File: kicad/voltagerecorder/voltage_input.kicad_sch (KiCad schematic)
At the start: 11 parts

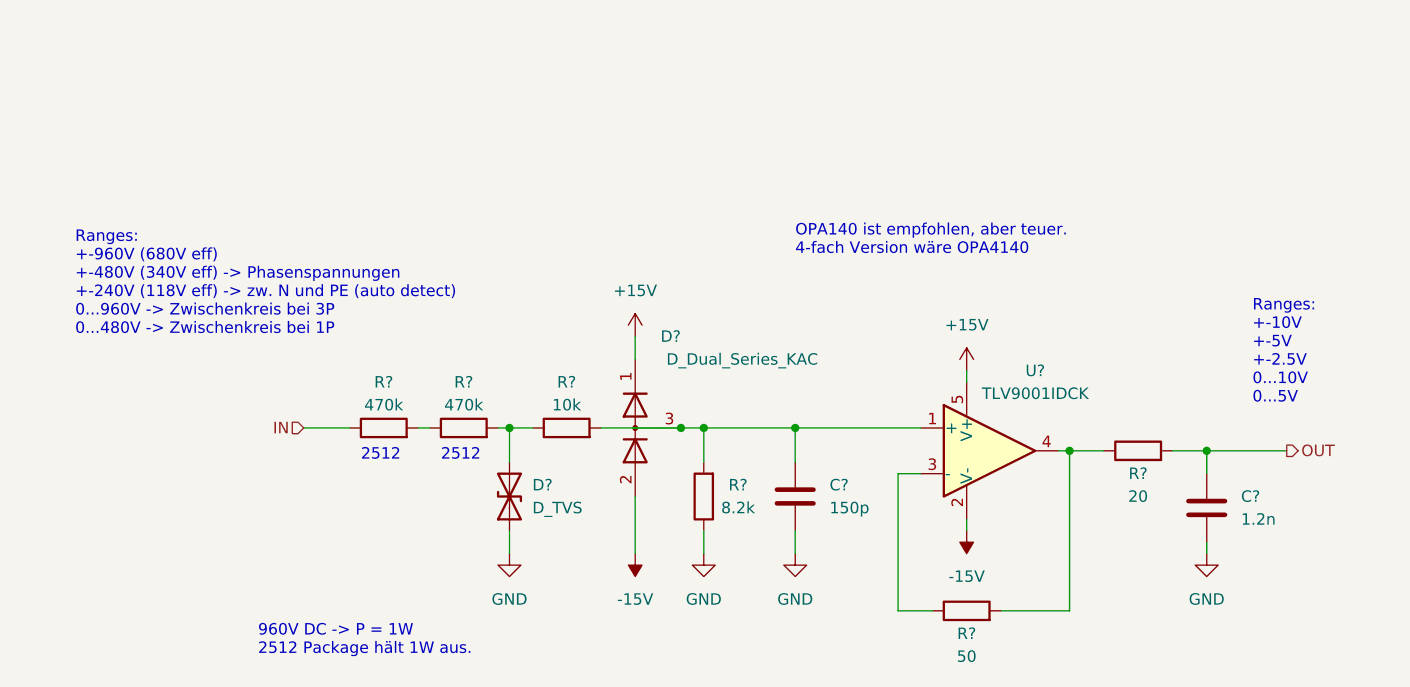
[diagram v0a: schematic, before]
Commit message: Schematic as pdf added.
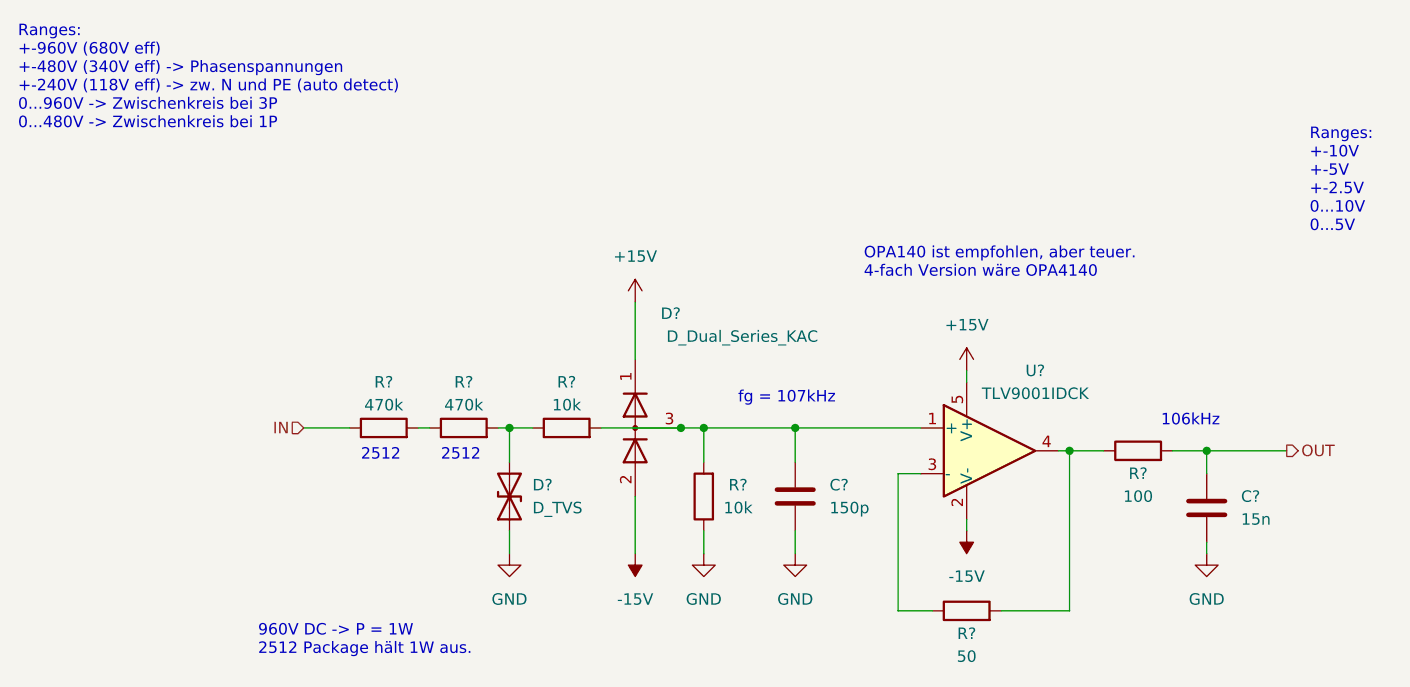
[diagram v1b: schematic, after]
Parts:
- C?: value 1.2n -> 15n
- R?: value 20 -> 100
- R?: value 8.2k -> 10k
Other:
- note added: "106kHz"
- note added: "fg = 107kHz"
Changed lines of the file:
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@@
     (stroke (width 0) (type default) (color 0 0 0 0))
   )
-  (wire (pts (xy 132.08 82.55) (xy 132.08 85.09))
+  (wire (pts (xy 132.08 78.74) (xy 132.08 85.09))
     (stroke (width 0) (type default) (color 0 0 0 0))
   )
@@
   )
   (text "Ranges:\n+-960V (680V eff)\n+-480V (340V eff) -> Phasenspannungen\n+-240V (118V eff) -> zw. N und PE (auto detect)\n0...960V -> Zwischenkreis bei 3P\n0...480V -> Zwischenkreis bei 1P\n"
-    (at 69.85 82.55 0)
+    (at 63.5 59.69 0)
     (effects (font (size 1.27 1.27)) (justify left bottom))
   )
@@
     (effects (font (size 1.27 1.27)) (justify left bottom))
   )
+  (text "106kHz" (at 190.5 92.71 0)
+    (effects (font (size 1.27 1.27)) (justify left bottom))
+  )
   (text "OPA140 ist empfohlen, aber teuer.\n4-fach Version wäre OPA4140"
-    (at 149.86 73.66 0)
-    (effects (font (size 1.27 1.27)) (justify left bottom))
-  )
-  (text "Ranges:\n+-10V\n+-5V\n+-2.5V\n0...10V\n0...5V" (at 200.66 90.17 0)
+    (at 157.48 76.2 0)
+    (effects (font (size 1.27 1.27)) (justify left bottom))
+  )
+  (text "Ranges:\n+-10V\n+-5V\n+-2.5V\n0...10V\n0...5V" (at 207.01 71.12 0)
     (effects (font (size 1.27 1.27)) (justify left bottom))
   )
   (text "2512" (at 110.49 96.52 0)
+    (effects (font (size 1.27 1.27)) (justify left bottom))
+  )
+  (text "fg = 107kHz" (at 143.51 90.17 0)
     (effects (font (size 1.27 1.27)) (justify left bottom))
   )
@@
     (pin "1")
   )
-  (symbol (lib_id "power:+15V") (at 132.08 82.55 0) (unit 1)
-    (in_bom yes) (on_board yes) (fields_autoplaced)
-    (property "Reference" "#PWR?" (id 0) (at 132.08 86.36 0)
-      (effects (font (size 1.27 1.27)) hide)
-    )
-    (property "Value" "+15V" (id 1) (at 132.08 77.47 0))
-    (property "Footprint" "" (id 2) (at 132.08 82.55 0)
-      (effects (font (size 1.27 1.27)) hide)
-    )
-    (property "Datasheet" "" (id 3) (at 132.08 82.55 0)
+  (symbol (lib_id "power:+15V") (at 132.08 78.74 0) (unit 1)
+    (in_bom yes) (on_board yes)
+    (property "Reference" "#PWR?" (id 0) (at 132.08 82.55 0)
+      (effects (font (size 1.27 1.27)) hide)
+    )
+    (property "Value" "+15V" (id 1) (at 132.08 73.66 0))
+    (property "Footprint" "" (id 2) (at 132.08 78.74 0)
+      (effects (font (size 1.27 1.27)) hide)
+    )
+    (property "Datasheet" "" (id 3) (at 132.08 78.74 0)
       (effects (font (size 1.27 1.27)) hide)
     )
@@
     (in_bom yes) (on_board yes)
     (property "Reference" "R?" (id 0) (at 187.96 97.79 90))
-    (property "Value" "20" (id 1) (at 187.96 100.33 90))
+    (property "Value" "100" (id 1) (at 187.96 100.33 90))
     (property "Footprint" "" (id 2) (at 187.96 97.028 90)
       (effects (font (size 1.27 1.27)) hide)
@@
       (effects (font (size 1.27 1.27)) (justify left))
     )
-    (property "Value" "1.2n" (id 1) (at 199.39 102.8699 0)
+    (property "Value" "15n" (id 1) (at 199.39 102.8699 0)
       (effects (font (size 1.27 1.27)) (justify left))
     )
@@
   (symbol (lib_id "Device:D_Dual_Series_KAC") (at 132.08 92.71 90) (unit 1)
     (in_bom yes) (on_board yes)
-    (property "Reference" "D?" (id 0) (at 137.16 82.55 90)
-      (effects (font (size 1.27 1.27)) (justify left))
-    )
-    (property "Value" "D_Dual_Series_KAC" (id 1) (at 152.4 85.09 90)
+    (property "Reference" "D?" (id 0) (at 137.16 80.01 90)
+      (effects (font (size 1.27 1.27)) (justify left))
+    )
+    (property "Value" "D_Dual_Series_KAC" (id 1) (at 152.4 82.55 90)
       (effects (font (size 1.27 1.27)) (justify left))
     )
@@
     (in_bom yes) (on_board yes)
     (property "Reference" "R?" (id 0) (at 143.51 99.06 0))
-    (property "Value" "8.2k" (id 1) (at 143.51 101.6 0))
+    (property "Value" "10k" (id 1) (at 143.51 101.6 0))
     (property "Footprint" "" (id 2) (at 141.478 100.33 90)
       (effects (font (size 1.27 1.27)) hide)

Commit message: BOM hinzugefügt, Schaltplan editiert.
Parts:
- removed R?: 10k, symbol Device:R
- added R?: 330k, symbol Device:R
- R? (x2): value 470k -> 330k
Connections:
- net at C?.1, D?.3 (common), R?.2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: now also D?.2 (A2), R?.2
- net at R?.2: now also R?.1; no longer D?.2 (A2)
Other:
- note added: "1000V DC -> P = 1W"
- note added: "MELF"
- note removed: "2512"
- note removed: "960V DC -> P = 1W 2512 Package hält 1W aus."
- moved on the sheet: D?, R?
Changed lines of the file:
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@@
 (kicad_sch (version 20211123) (generator eeschema)
   (paper "A4")
-  (junction (at 118.11 92.71) (diameter 0) (color 0 0 0 0)
+  (junction (at 120.65 92.71) (diameter 0) (color 0 0 0 0)
   )
   (junction (at 149.86 92.71) (diameter 0) (color 0 0 0 0)
@@
   (junction (at 195.58 95.25) (diameter 0) (color 0 0 0 0)
   )
+  (wire (pts (xy 120.65 92.71) (xy 137.16 92.71))
+    (stroke (width 0) (type default) (color 0 0 0 0))
+  )
   (wire (pts (xy 180.34 95.25) (xy 184.15 95.25))
     (stroke (width 0) (type default) (color 0 0 0 0))
@@
     (stroke (width 0) (type default) (color 0 0 0 0))
   )
-  (wire (pts (xy 95.25 92.71) (xy 100.33 92.71))
+  (wire (pts (xy 120.65 92.71) (xy 120.65 96.52))
+    (stroke (width 0) (type default) (color 0 0 0 0))
+  )
+  (wire (pts (xy 83.82 92.71) (xy 88.9 92.71))
     (stroke (width 0) (type default) (color 0 0 0 0))
   )
@@
     (stroke (width 0) (type default) (color 0 0 0 0))
   )
-  (wire (pts (xy 118.11 104.14) (xy 118.11 106.68))
+  (wire (pts (xy 120.65 104.14) (xy 120.65 106.68))
     (stroke (width 0) (type default) (color 0 0 0 0))
   )
@@
     (stroke (width 0) (type default) (color 0 0 0 0))
   )
+  (wire (pts (xy 105.41 92.71) (xy 106.68 92.71))
+    (stroke (width 0) (type default) (color 0 0 0 0))
+  )
   (wire (pts (xy 195.58 95.25) (xy 195.58 97.79))
     (stroke (width 0) (type default) (color 0 0 0 0))
   )
-  (wire (pts (xy 107.95 92.71) (xy 109.22 92.71))
+  (wire (pts (xy 96.52 92.71) (xy 97.79 92.71))
     (stroke (width 0) (type default) (color 0 0 0 0))
   )
@@
     (stroke (width 0) (type default) (color 0 0 0 0))
   )
-  (wire (pts (xy 116.84 92.71) (xy 118.11 92.71))
-    (stroke (width 0) (type default) (color 0 0 0 0))
-  )
   (wire (pts (xy 161.29 113.03) (xy 165.1 113.03))
     (stroke (width 0) (type default) (color 0 0 0 0))
   )
-  (wire (pts (xy 118.11 92.71) (xy 118.11 96.52))
-    (stroke (width 0) (type default) (color 0 0 0 0))
-  )
-  (wire (pts (xy 128.27 92.71) (xy 137.16 92.71))
-    (stroke (width 0) (type default) (color 0 0 0 0))
-  )
   (wire (pts (xy 180.34 113.03) (xy 180.34 95.25))
     (stroke (width 0) (type default) (color 0 0 0 0))
   )
+  (wire (pts (xy 114.3 92.71) (xy 120.65 92.71))
+    (stroke (width 0) (type default) (color 0 0 0 0))
+  )
   (wire (pts (xy 172.72 113.03) (xy 180.34 113.03))
     (stroke (width 0) (type default) (color 0 0 0 0))
@@
     (stroke (width 0) (type default) (color 0 0 0 0))
   )
-  (wire (pts (xy 118.11 92.71) (xy 120.65 92.71))
-    (stroke (width 0) (type default) (color 0 0 0 0))
-  )
   (wire (pts (xy 149.86 92.71) (xy 163.83 92.71))
     (stroke (width 0) (type default) (color 0 0 0 0))
   )
-  (text "2512" (at 101.6 96.52 0)
+  (text "MELF" (at 90.17 96.52 0)
     (effects (font (size 1.27 1.27)) (justify left bottom))
   )
@@
     (effects (font (size 1.27 1.27)) (justify left bottom))
   )
-  (text "960V DC -> P = 1W\n2512 Package hält 1W aus." (at 90.17 118.11 0)
+  (text "MELF" (at 140.97 105.41 0)
+    (effects (font (size 1.27 1.27)) (justify left bottom))
+  )
+  (text "1000V DC -> P = 1W" (at 88.9 102.87 0)
     (effects (font (size 1.27 1.27)) (justify left bottom))
   )
   (text "106kHz" (at 190.5 92.71 0)
+    (effects (font (size 1.27 1.27)) (justify left bottom))
+  )
+  (text "MELF" (at 107.95 96.52 0)
     (effects (font (size 1.27 1.27)) (justify left bottom))
   )
@@
     (effects (font (size 1.27 1.27)) (justify left bottom))
   )
-  (text "2512" (at 110.49 96.52 0)
+  (text "MELF" (at 99.06 96.52 0)
     (effects (font (size 1.27 1.27)) (justify left bottom))
   )
@@
     (effects (font (size 1.27 1.27)) (justify left bottom))
   )
-  (hierarchical_label "IN" (shape input) (at 95.25 92.71 180)
+  (hierarchical_label "IN" (shape input) (at 83.82 92.71 180)
     (effects (font (size 1.27 1.27)) (justify right))
   )
@@
     (pin "2")
   )
-  (symbol (lib_id "Device:D_TVS") (at 118.11 100.33 90) (unit 1)
-    (in_bom yes) (on_board yes) (fields_autoplaced)
-    (property "Reference" "D?" (id 0) (at 120.65 99.0599 90)
+  (symbol (lib_id "Device:D_TVS") (at 120.65 100.33 90) (unit 1)
+    (in_bom yes) (on_board yes) (fields_autoplaced)
+    (property "Reference" "D?" (id 0) (at 123.19 99.0599 90)
       (effects (font (size 1.27 1.27)) (justify right))
     )
-    (property "Value" "D_TVS" (id 1) (at 120.65 101.5999 90)
+    (property "Value" "D_TVS" (id 1) (at 123.19 101.5999 90)
       (effects (font (size 1.27 1.27)) (justify right))
     )
-    (property "Footprint" "" (id 2) (at 118.11 100.33 0)
-      (effects (font (size 1.27 1.27)) hide)
-    )
-    (property "Datasheet" "~" (id 3) (at 118.11 100.33 0)
+    (property "Footprint" "" (id 2) (at 120.65 100.33 0)
+      (effects (font (size 1.27 1.27)) hide)
+    )
+    (property "Datasheet" "~" (id 3) (at 120.65 100.33 0)
       (effects (font (size 1.27 1.27)) hide)
     )
@@
     (pin "1")
   )
-  (symbol (lib_id "power:GND") (at 118.11 106.68 0) (unit 1)
-    (in_bom yes) (on_board yes) (fields_autoplaced)
-    (property "Reference" "#PWR?" (id 0) (at 118.11 113.03 0)
-      (effects (font (size 1.27 1.27)) hide)
-    )
-    (property "Value" "GND" (id 1) (at 118.11 111.76 0))
-    (property "Footprint" "" (id 2) (at 118.11 106.68 0)
-      (effects (font (size 1.27 1.27)) hide)
-    )
-    (property "Datasheet" "" (id 3) (at 118.11 106.68 0)
+  (symbol (lib_id "power:GND") (at 120.65 106.68 0) (unit 1)
+    (in_bom yes) (on_board yes) (fields_autoplaced)
+    (property "Reference" "#PWR?" (id 0) (at 120.65 113.03 0)
+      (effects (font (size 1.27 1.27)) hide)
+    )
+    (property "Value" "GND" (id 1) (at 120.65 111.76 0))
+    (property "Footprint" "" (id 2) (at 120.65 106.68 0)
+      (effects (font (size 1.27 1.27)) hide)
+    )
+    (property "Datasheet" "" (id 3) (at 120.65 106.68 0)
       (effects (font (size 1.27 1.27)) hide)
     )
@@
     (pin "2")
   )
-  (symbol (lib_id "Device:R") (at 113.03 92.71 90) (unit 1)
-    (in_bom yes) (on_board yes)
-    (property "Reference" "R?" (id 0) (at 113.03 87.63 90))
-    (property "Value" "470k" (id 1) (at 113.03 90.17 90))
-    (property "Footprint" "" (id 2) (at 113.03 94.488 90)
-      (effects (font (size 1.27 1.27)) hide)
-    )
-    (property "Datasheet" "~" (id 3) (at 113.03 92.71 0)
-      (effects (font (size 1.27 1.27)) hide)
-    )
-    (pin "1")
-    (pin "2")
-  )
-  (symbol (lib_id "Device:R") (at 124.46 92.71 90) (unit 1)
-    (in_bom yes) (on_board yes)
-    (property "Reference" "R?" (id 0) (at 124.46 87.63 90))
-    (property "Value" "10k" (id 1) (at 124.46 90.17 90))
-    (property "Footprint" "" (id 2) (at 124.46 94.488 90)
-      (effects (font (size 1.27 1.27)) hide)
-    )
-    (property "Datasheet" "~" (id 3) (at 124.46 92.71 0)
+  (symbol (lib_id "Device:R") (at 101.6 92.71 90) (unit 1)
+    (in_bom yes) (on_board yes)
+    (property "Reference" "R?" (id 0) (at 101.6 87.63 90))
+    (property "Value" "330k" (id 1) (at 101.6 90.17 90))
+    (property "Footprint" "" (id 2) (at 101.6 94.488 90)
+      (effects (font (size 1.27 1.27)) hide)
+    )
+    (property "Datasheet" "~" (id 3) (at 101.6 92.71 0)
       (effects (font (size 1.27 1.27)) hide)
     )
@@
     (pin "1")
   )
-  (symbol (lib_id "Device:R") (at 104.14 92.71 90) (unit 1)
-    (in_bom yes) (on_board yes)
-    (property "Reference" "R?" (id 0) (at 104.14 87.63 90))
-    (property "Value" "470k" (id 1) (at 104.14 90.17 90))
-    (property "Footprint" "" (id 2) (at 104.14 94.488 90)
-      (effects (font (size 1.27 1.27)) hide)
-    )
-    (property "Datasheet" "~" (id 3) (at 104.14 92.71 0)
+  (symbol (lib_id "Device:R") (at 92.71 92.71 90) (unit 1)
+    (in_bom yes) (on_board yes)
+    (property "Reference" "R?" (id 0) (at 92.71 87.63 90))
+    (property "Value" "330k" (id 1) (at 92.71 90.17 90))
+    (property "Footprint" "" (id 2) (at 92.71 94.488 90)
+      (effects (font (size 1.27 1.27)) hide)
+    )
+    (property "Datasheet" "~" (id 3) (at 92.71 92.71 0)
       (effects (font (size 1.27 1.27)) hide)
     )
@@
       (effects (font (size 1.27 1.27)) hide)
     )
+    (pin "1")
+    (pin "2")
+  )
+  (symbol (lib_id "Device:R") (at 110.49 92.71 90) (unit 1)
+    (in_bom yes) (on_board yes)
+    (property "Reference" "R?" (id 0) (at 110.49 87.63 90))
+    (property "Value" "330k" (id 1) (at 110.49 90.17 90))
+    (property "Footprint" "" (id 2) (at 110.49 94.488 90)
+      (effects (font (size 1.27 1.27)) hide)
+    )
+    (property "Datasheet" "~" (id 3) (at 110.49 92.71 0)
+      (effects (font (size 1.27 1.27)) hide)
+    )

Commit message: a
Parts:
- added R?: 1k, symbol Device:R
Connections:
- net at C?.1, D?.3 (common), R?.2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: now also R?.2; no longer D?.2 (A2), U?.1 (+)
- new net: R?.1, U?.1 (+)
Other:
- moved on the sheet: C?, D?, R?

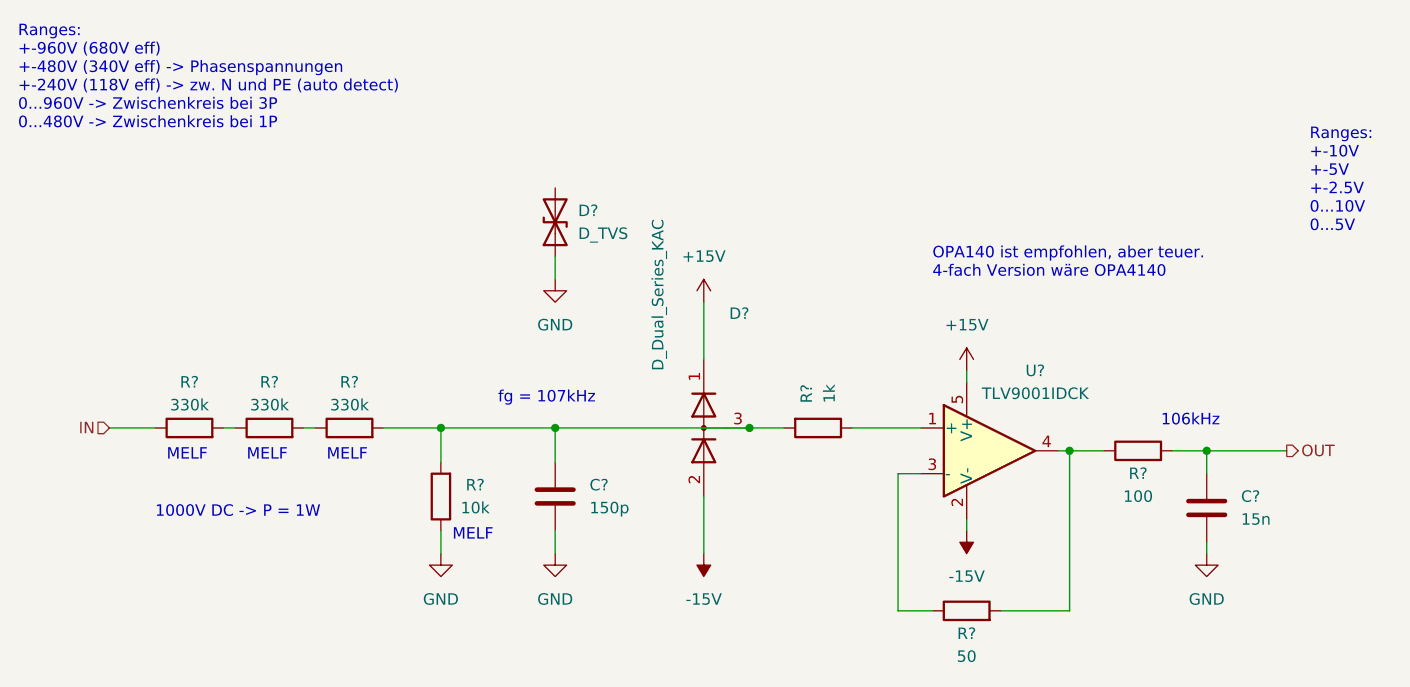
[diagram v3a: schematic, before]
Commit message: current_addon_single erstellt. Schaltplan aktualisiert.
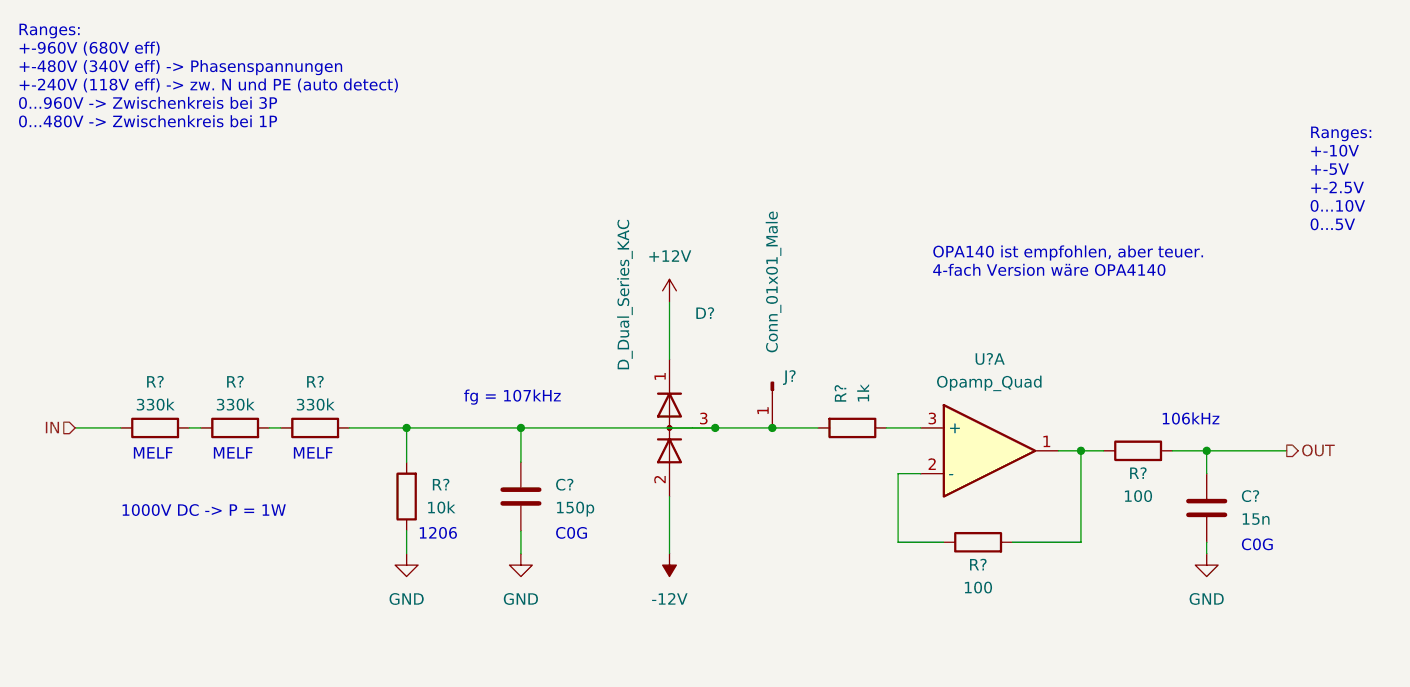
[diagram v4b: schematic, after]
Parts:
- removed D?: D_TVS, symbol Device:D_TVS
- removed U?: TLV9001IDCK, Package_TO_SOT_SMD:SOT-353_SC-70-5, symbol Amplifier_Operational:TLV9001IDCK
- added J?: Conn_01x01_Male, symbol Connector:Conn_01x01_Male
- added U?: Opamp_Quad, symbol Device:Opamp_Quad
- R?: value 50 -> 100
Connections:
- net at C?.1, D?.3 (common), R?.2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: now also J?.1 (Pin_1)
- net at R?.1: now also U?.2 (-)
- net at R?.1, R?.2: now also U?.1
- net at R?.1: now also U?.3 (+)
- net +15V renamed +12V
- net -15V renamed -12V
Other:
- note added: "1206"
- note added: "C0G"
- moved on the sheet: C?, D?, R?
